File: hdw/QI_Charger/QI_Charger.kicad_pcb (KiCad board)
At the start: 2 copper layers, 278 parts, among them J1001 USB_B_Mini, J1301 PAD, J1302 PAD, J201 +12V IN, Q201 IPC100N04S51R7ATMA1, Q202 IPC100N04S51R7ATMA1, Q401 BSS214NW, SW401 MRST, SW801 Cap_Touch, SW802 Cap_Touch, U1001 LT6700-1-S6, U1002 FT234XD, U1003 74LVC1G06, U1004 TPD3S014DBVR, U1101 74LVC1G06, U1102 74LVC1G07, U1103 74LVC1G07, U1104 74LVC1G06, U1105 74LVC1G07, U1106 74LVC1G06, U1107 74LVC1G06, U1108 74LVC1G06, U1109 74LVC1G06, U1302 NXQ1TXH5_101J, U1401 74LVC1G14, U1402 74LVC1G14, U1403 74LVC1G17, U201 LTC4365DDB, U302 74LVC1G17, U501 74LVC1G17, U502 74LVC1G17, U503 PIC18F27K40T-I_ML, U701 SSD1306, U801 AT42QT1010-TSHR, U802 AT42QT1010-TSHR, U901 ISO7321C, Y1301 32.768kHz, Y501 16MHz

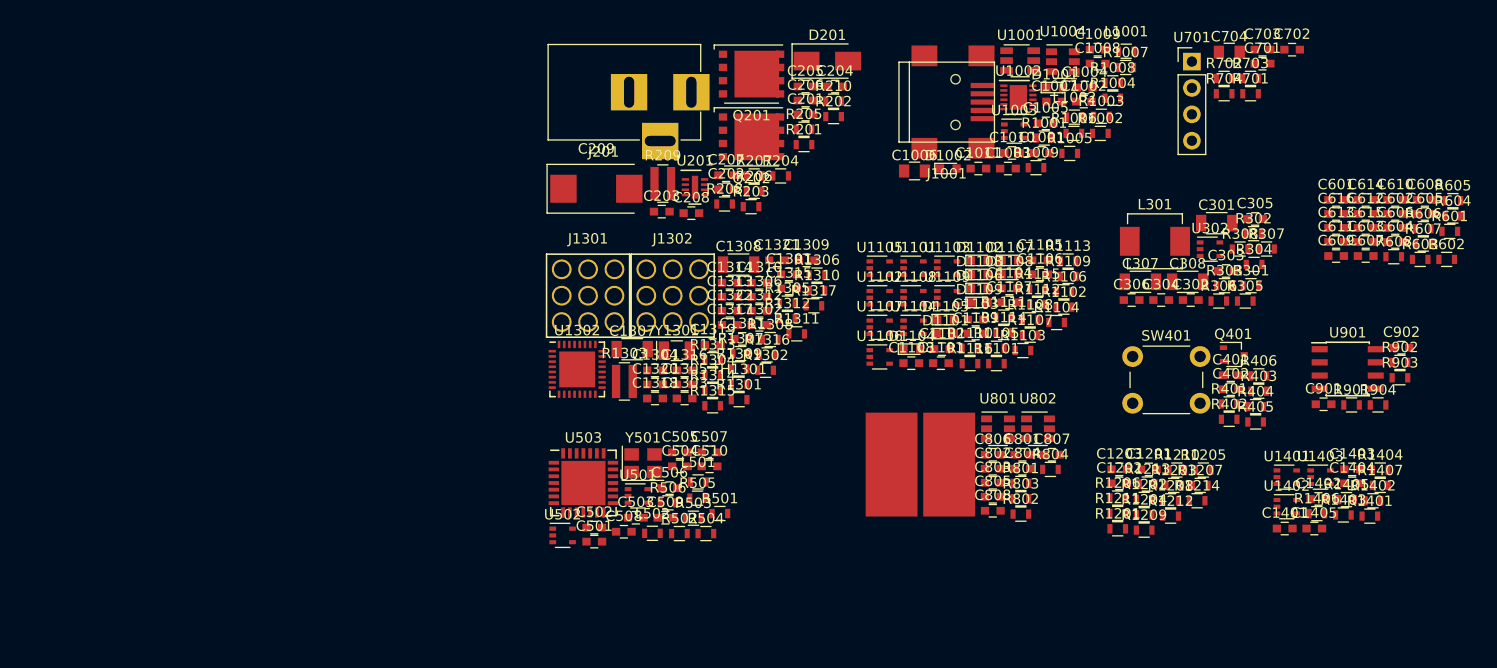
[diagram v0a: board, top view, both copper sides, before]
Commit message: Fixed some footprint issues
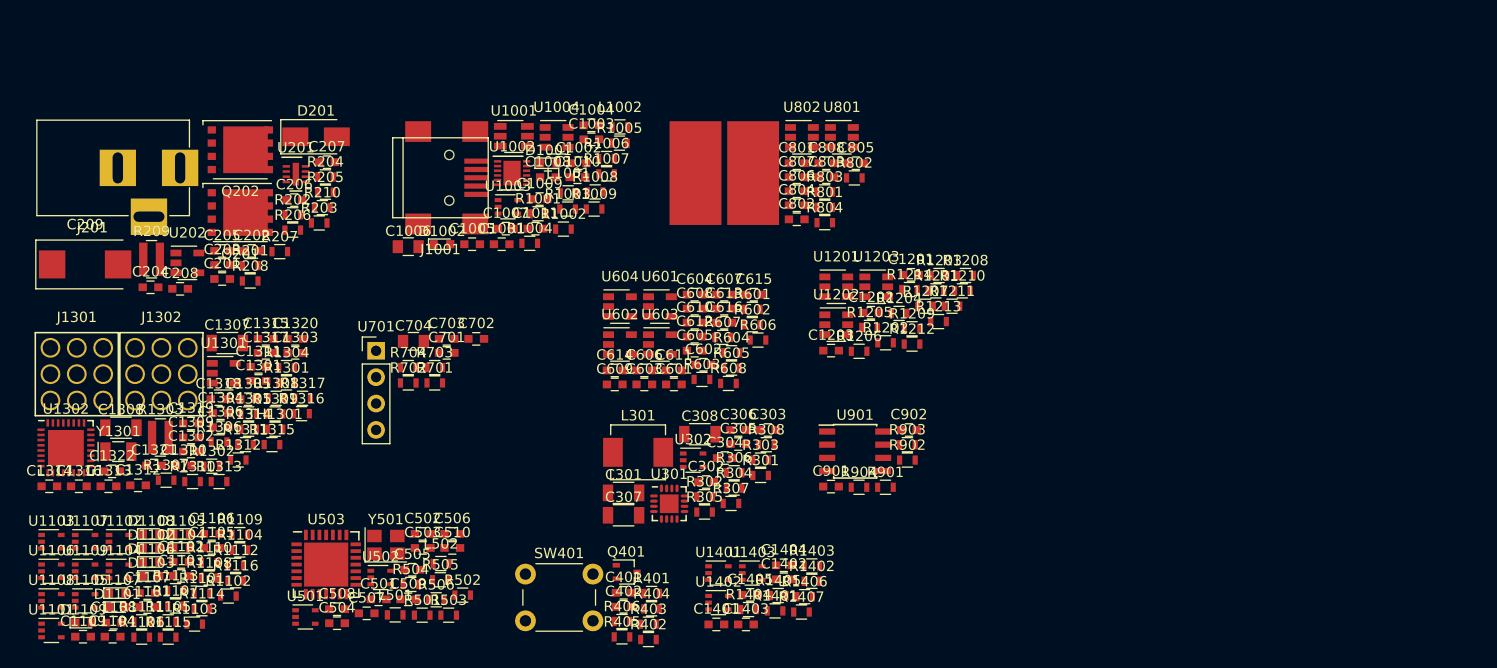
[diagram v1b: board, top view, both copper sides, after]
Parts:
- added U1201: LM73-1, TO_SOT_Packages_SMD:SOT-23-6, F.Cu at (194.7, 91.1)
- added U1202: LM73-1, TO_SOT_Packages_SMD:SOT-23-6, F.Cu at (194.7, 94.8)
- added U1203: LM73-1, TO_SOT_Packages_SMD:SOT-23-6, F.Cu at (198.6, 91.1)
- added U1301: INA138, TO_SOT_Packages_SMD:SOT-23-5, F.Cu at (135.7, 99.4)
- added U202: INA138, TO_SOT_Packages_SMD:SOT-23-5, F.Cu at (132.2, 88.8)
- added U301: TPS62130, Housings_DFN_QFN:QFN-16-1EP_3x3mm_Pitch0.5mm, F.Cu at (178.6, 112.0)
- added U601: OPA340NA, TO_SOT_Packages_SMD:SOT-23-5, F.Cu at (177.7, 93.0)
- added U602: OPA340NA, TO_SOT_Packages_SMD:SOT-23-5, F.Cu at (173.9, 96.7)
- added U603: OPA340NA, TO_SOT_Packages_SMD:SOT-23-5, F.Cu at (177.7, 96.7)
- added U604: OPA340NA, TO_SOT_Packages_SMD:SOT-23-5, F.Cu at (173.9, 93.0)
- moved R1106 94.9 mm to (127.8, 124.9)
- moved C1104 92.7 mm to (125.0, 124.8)
- moved D1107 91.8 mm to (125.5, 120.6)
- moved R1113 91.7 mm to (131.1, 120.4)
- moved D1109 91.6 mm to (122.2, 123.5)
- moved C1109 90.8 mm to (122.2, 124.8)
- moved U1103 90.2 mm to (119.1, 115.7)
- moved R1115 90.2 mm to (130.4, 124.9)
- moved U1101 90.1 mm to (119.1, 124.2)
- moved R1111 88.1 mm to (127.8, 123.4)
- moved U1108 88.0 mm to (119.1, 121.4)
- moved C1107 87.6 mm to (128.4, 120.6)
- moved U1109 87.1 mm to (122.4, 118.5)
- moved D1108 86.4 mm to (128.7, 114.9)
- moved R1107 86.4 mm to (131.1, 121.9)
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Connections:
- C302 pad 1: (no net) -> Net-(C302-Pad1)
- R1213 pad 1: (no net) -> Net-(R1213-Pad1)
- R1214 pad 2: (no net) -> Net-(R1214-Pad2)
- R603 pad 2: (no net) -> Net-(R603-Pad2)
- R604 pad 2: (no net) -> Net-(R604-Pad2)
- R605 pad 2: (no net) -> Net-(R605-Pad2)
- R608 pad 2: (no net) -> Net-(R608-Pad2)

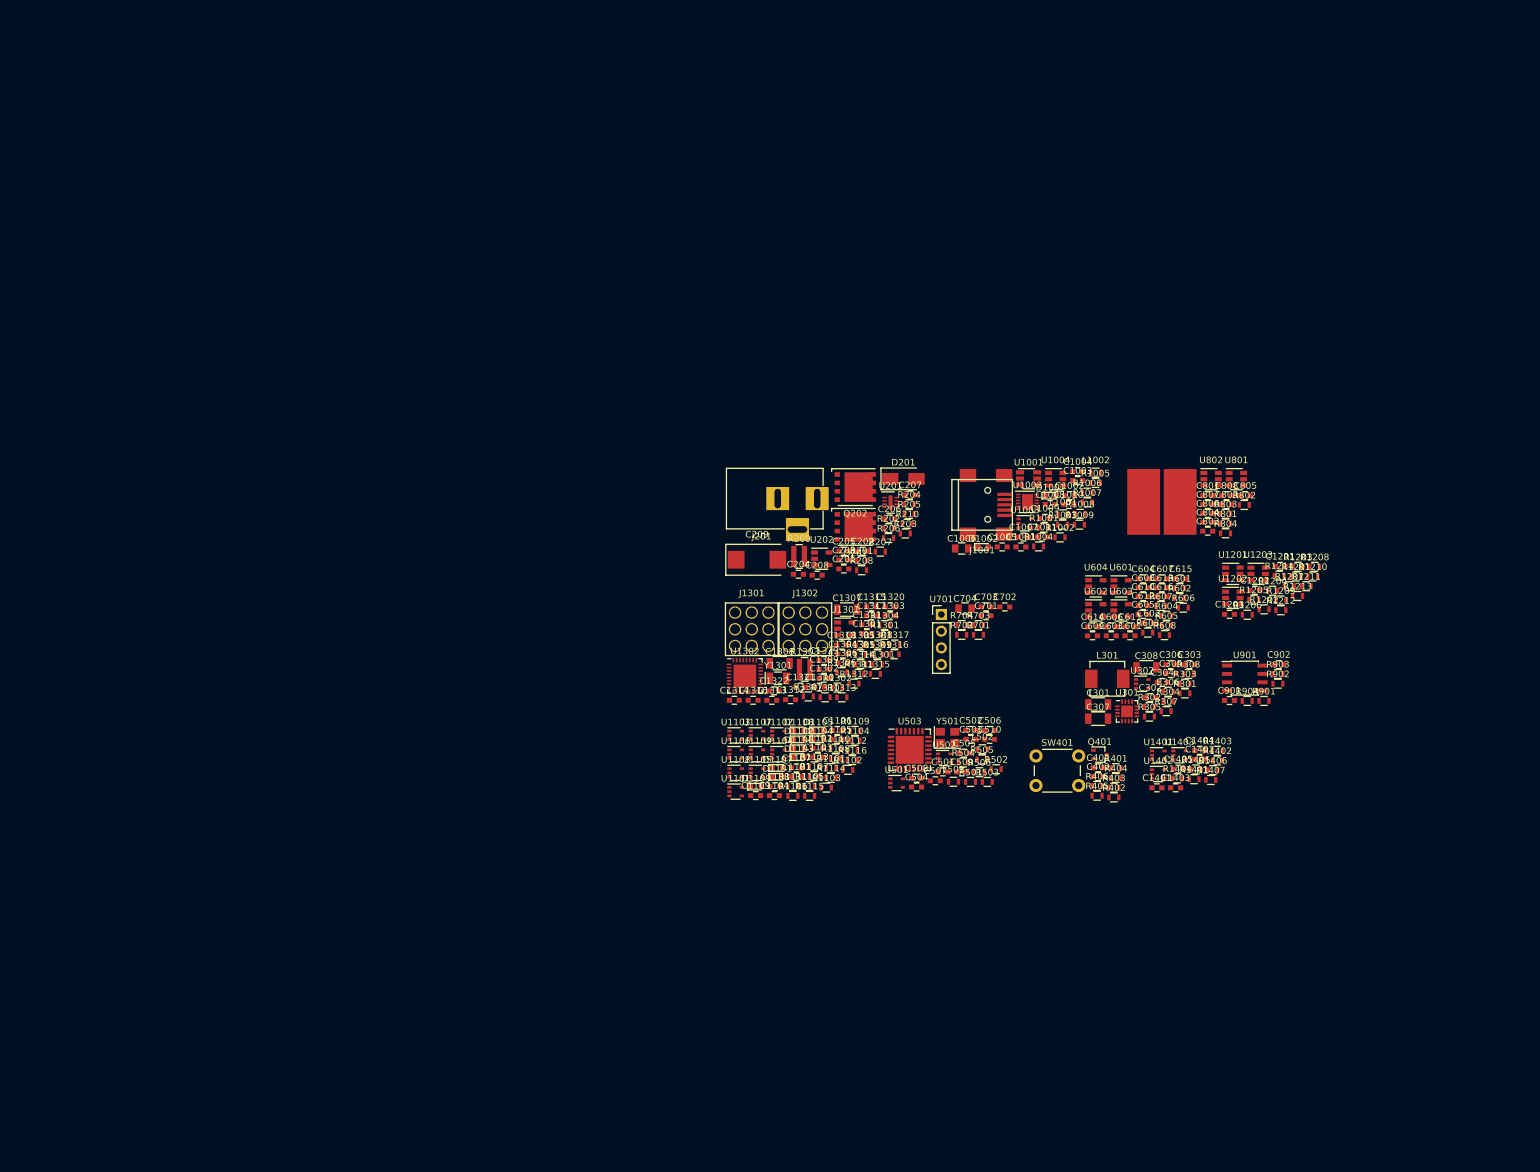
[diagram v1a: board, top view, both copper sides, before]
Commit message: Arranged a lot of parts on PCB
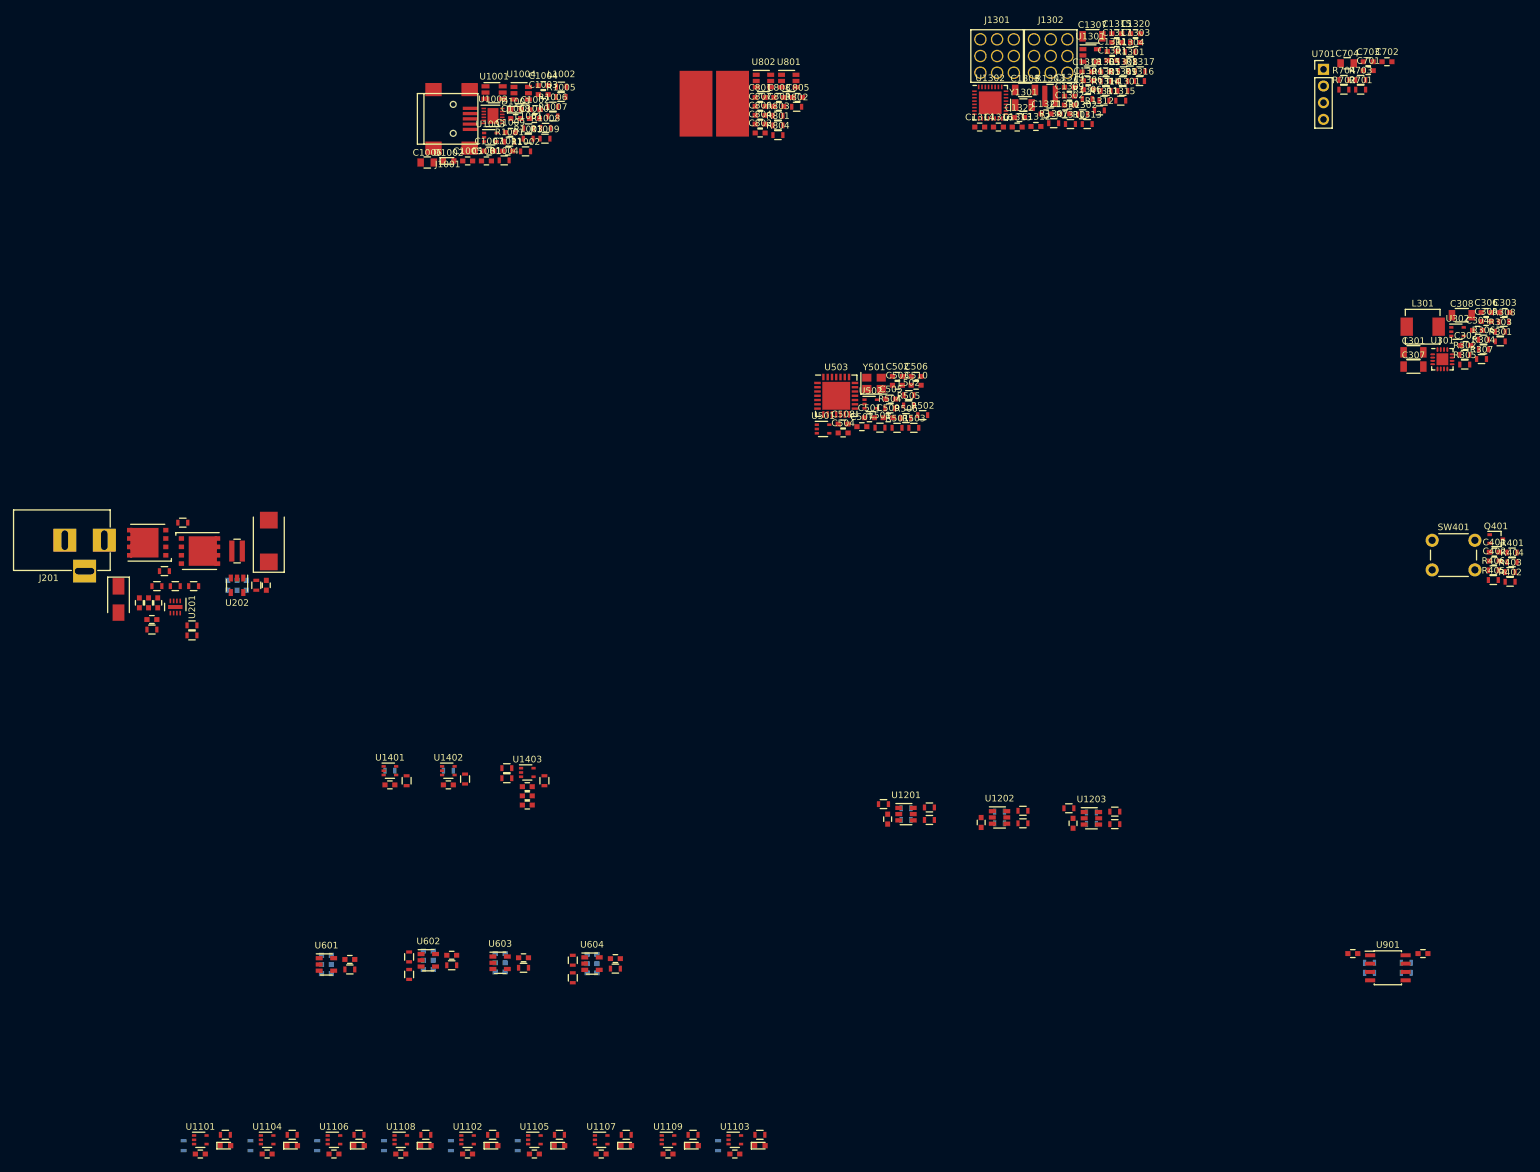
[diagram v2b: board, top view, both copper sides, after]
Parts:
- C205, C206, C207, C601, C602, C603, C604, C605, C606, C609, C610, C611, C613, C614, C615, R1101, R1102, R1103, R1107, R1108, R1111, R1114, R1207, R1208, R1209, R1210, R1211, R1212, R1401, R1402, R901, R902, R903, R904: moved to B.Cu
- moved C607 136.4 mm to (60.5, 149.7), turned to 180 degrees
- moved C605 135.7 mm to (56.9, 151.9), turned to 180 degrees
- moved U601 133.8 mm to (56.9, 150.5)
- moved R603 131.7 mm to (60.5, 151.3), turned to 180 degrees
- moved C601 131.5 mm to (56.9, 149.1), turned to 180 degrees
- moved R602 130.4 mm to (69.5, 152.0), turned to 90 degrees
- moved R601 129.9 mm to (69.5, 149.4), turned to 90 degrees
- moved C603 129.4 mm to (56.9, 150.5), turned to 180 degrees
- moved C604 123.2 mm to (72.4, 149.9), turned to 180 degrees
- moved R1406 122.6 mm to (69.1, 122.6), turned to 90 degrees
- moved R1401 122.3 mm to (66.5, 121.0)
- moved R604 121.0 mm to (75.9, 150.6)
- moved D201 120.8 mm to (25.3, 95.0), turned to 270 degrees
- moved C602 120.4 mm to (72.4, 148.5), turned to 180 degrees
- moved C1403 119.5 mm to (66.5, 123.2), turned to 180 degrees
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
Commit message: Placed more parts
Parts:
- added J401: PICKIT3, Custom Footprints Library:PICKIT3_Header, F.Cu at (243.1, 86.4)
- C803, C804, C805, C806, C807, C808: moved to B.Cu
- R1207, R1208, R1209, R1210, R1211, R1212: moved to F.Cu
- moved R303 225.9 mm to (23.7, 133.3), turned to 180 degrees
- moved C303 225.2 mm to (22.9, 123.8), turned to 90 degrees
- moved R302 219.1 mm to (23.7, 131.8)
- moved C308 215.7 mm to (28.7, 130.4), turned to 180 degrees
- moved C302 215.1 mm to (25.4, 122.4)
- moved R301 214.7 mm to (31.2, 122.0), turned to 270 degrees
- moved R307 214.3 mm to (27.9, 122.0), turned to 90 degrees
- moved R306 213.9 mm to (29.6, 122.0), turned to 270 degrees
- moved C301 211.5 mm to (22.9, 128.0), turned to 270 degrees
- moved U301 210.9 mm to (26.8, 125.9), turned to 180 degrees
- moved R304 208.0 mm to (35.7, 123.1)
- moved R308 207.7 mm to (38.7, 118.0)
- moved C307 206.9 mm to (28.7, 132.7), turned to 180 degrees
- moved C306 206.0 mm to (39.2, 120.5), turned to 270 degrees
- moved C305 204.2 mm to (40.6, 120.5), turned to 270 degrees
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
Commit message: Added test points, arranged more parts on PCB
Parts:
- added D1301: MBR0530, Diodes_SMD:D_SOD-123, F.Cu at (89.8, 99.8)
- added TP1001: TP, Custom Footprints Library:Test_Point, F.Cu at (246.7, 171.6)
- added TP1002: TP, Pin_Headers:Pin_Header_Angled_1x01_Pitch2.54mm, F.Cu at (246.7, 167.9)
- added TP201: TP, Pin_Headers:Pin_Header_Angled_1x01_Pitch2.54mm, F.Cu at (34.5, 73.3)
- added TP202: TP, Custom Footprints Library:Test_Point, F.Cu at (34.5, 77.0)
- added TP203: TP, Custom Footprints Library:Test_Point, F.Cu at (38.2, 77.0)
- added TP301: TP, Custom Footprints Library:Test_Point, F.Cu at (41.3, 129.3)
- C1001, C1002, C1004, C1006, C1007, C1009, C1010, C1301, C1302, C1304, C1313, C1315, R1001, R1007, R1008, R1312, R1313, TH1301, U1002: moved to B.Cu
- moved R401 233.4 mm to (13.6, 154.7), turned to 90 degrees
- moved R404 232.1 mm to (15.1, 156.8)
- moved R402 230.4 mm to (15.1, 154.7), turned to 270 degrees
- moved C402 229.3 mm to (16.4, 159.9)
- moved R403 228.8 mm to (17.8, 156.8)
- moved R405 227.8 mm to (16.4, 158.4), turned to 180 degrees
- moved Q401 227.7 mm to (17.8, 154.7)
- moved J1001 225.8 mm to (260.7, 151.6), turned to 180 degrees
- moved R406 225.7 mm to (19.1, 158.4), turned to 180 degrees
- moved SW401 223.1 mm to (9.14, 142.4)
- moved J401 221.5 mm to (31.2, 151.1)
- moved C401 218.7 mm to (28.1, 160.0), turned to 90 degrees
- moved U1004 213.9 mm to (250.4, 155.4), turned to 90 degrees
- moved L1001 212.9 mm to (255.4, 154.4), turned to 270 degrees
- moved C1011 212.0 mm to (253.7, 154.4), turned to 90 degrees
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
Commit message: Added mounting holes, board outline
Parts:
- added H1501: 3mm Mounting Hole, Mounting_Holes:MountingHole_3mm_Pad_Via, F.Cu at (5.08, -44.9)
- added H1502: 3mm Mounting Hole, Mounting_Holes:MountingHole_3mm_Pad_Via, F.Cu at (5.08, -5.08)
- added H1503: 3mm Mounting Hole, Mounting_Holes:MountingHole_3mm_Pad_Via, F.Cu at (51.7, -44.9)
- added H1504: 3mm Mounting Hole, Mounting_Holes:MountingHole_3mm_Pad_Via, F.Cu at (51.7, -5.08)
- added H1505: 3mm Mounting Hole, Mounting_Holes:MountingHole_3mm_Pad_Via, F.Cu at (98.3, -44.9)
- added H1506: 3mm Mounting Hole, Mounting_Holes:MountingHole_3mm_Pad_Via, F.Cu at (98.3, -5.08)
- added H1507: 3mm Mounting Hole, Mounting_Holes:MountingHole_3mm_Pad_Via, F.Cu at (144.9, -44.9)
- added H1508: 3mm Mounting Hole, Mounting_Holes:MountingHole_3mm_Pad_Via, F.Cu at (144.9, -5.08)
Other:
- board outline added: 150 x 50 mm

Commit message: Finished initial placement of parts
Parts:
- added C1323: 100uF, Capacitors_Tantalum_SMD:CP_Tantalum_Case-X_EIA-7343-43_Reflow, F.Cu at (169.9, 60.8)
- C1201, C1202, C1306, C502, C503, C608, C612, D201, R1201, R1202, R1203, R1204, R1207, R1208, R1210, R1211, R1213, R1304, R505, R506, R604, R605, U1201, U1202, U1301, U501, U502: moved to B.Cu
- moved J1001 228.5 mm to (43.6, 80.6), turned to 0 degrees
- moved L1001 220.2 mm to (48.9, 77.9), turned to 90 degrees
- moved C1011 217.2 mm to (50.5, 77.9), turned to 270 degrees
- moved L1002 216.6 mm to (48.9, 83.4), turned to 270 degrees
- moved U1004 211.7 mm to (53.8, 76.8), turned to 270 degrees
- moved C1008 211.0 mm to (53.0, 80.3), turned to 270 degrees
- moved TP1001 210.3 mm to (51.3, 93.9)
- moved C1005 210.3 mm to (51.3, 86.4), turned to 0 degrees
- moved U1003 209.1 mm to (51.3, 88.5), turned to 180 degrees
- moved R1004 204.9 mm to (54.9, 83.9), turned to 90 degrees
- moved R1005 204.3 mm to (54.0, 87.9), turned to 270 degrees
- moved R1003 200.1 mm to (57.1, 84.7), turned to 180 degrees
- moved R1001 199.3 mm to (61.3, 75.1), turned to 270 degrees
- moved C1010 198.6 mm to (60.3, 78.4), turned to 0 degrees
- moved U1001 198.4 mm to (57.1, 87.5), turned to 180 degrees
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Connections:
- U503 pad 27: Cap_Touch_Left -> POS12_ADC
- U503 pad 28: Cap_Touch_Right -> POS12_ISNS_ADC
- U503 pad 8: POS12_ADC -> Cap_Touch_Left
- U503 pad 9: POS12_ISNS_ADC -> Cap_Touch_Right
